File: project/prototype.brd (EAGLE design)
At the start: 76.2 x 38.1 mm, 10 parts, among them M1 NX7002AK, M2 NX3008PBK

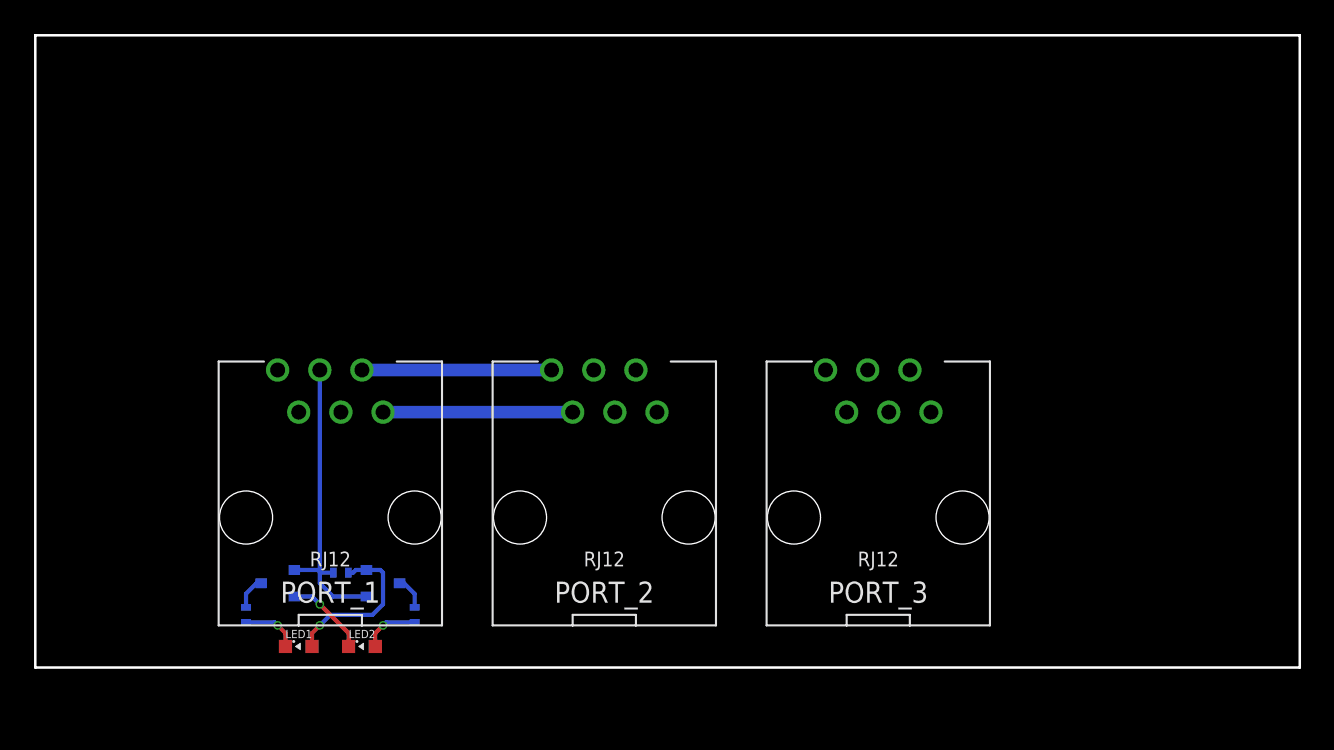
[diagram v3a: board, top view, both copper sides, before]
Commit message: Add input terminal blocks
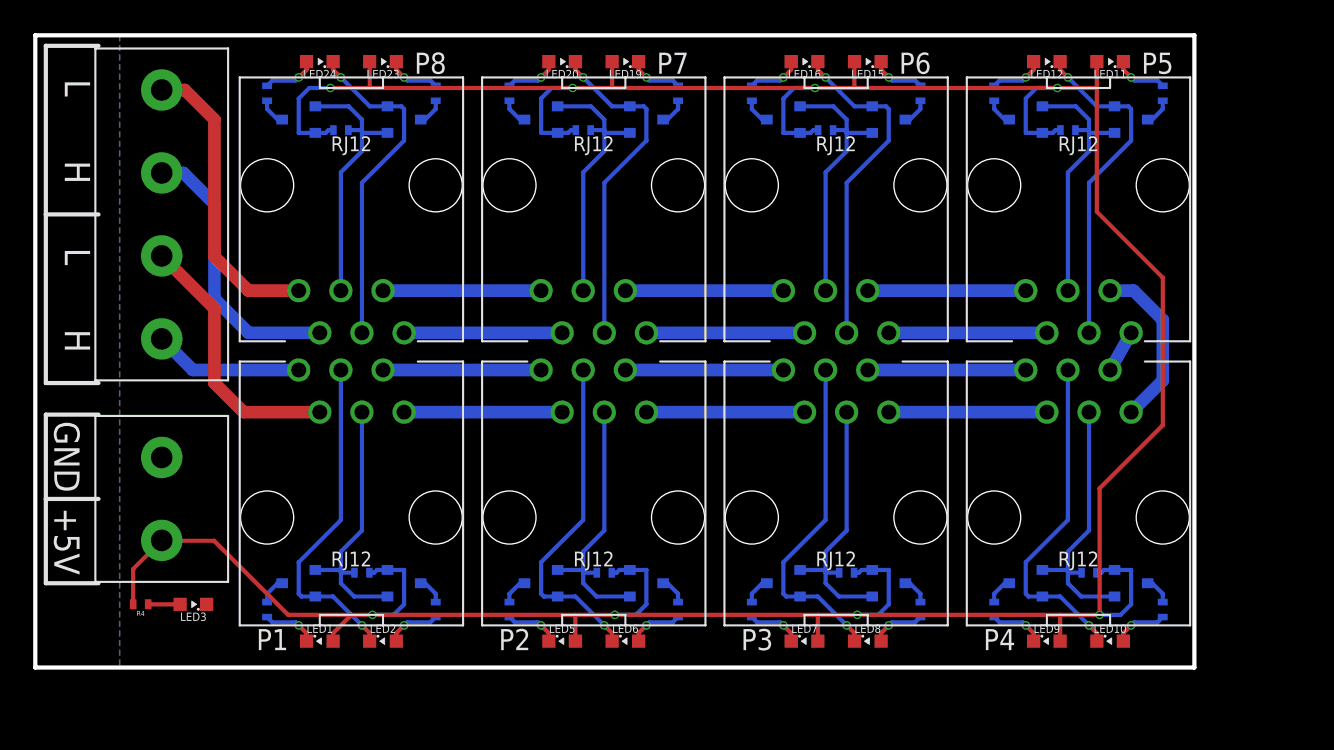
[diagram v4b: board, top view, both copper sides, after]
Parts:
- removed PORT_1, PORT_2, PORT_3: RJ12, components:RJ12
- added LED10, LED12, LED16, LED20, LED24, LED3, LED6, LED8: GREEN, components:0603-LED
- added LED11, LED15, LED19, LED23, LED5, LED7, LED9: RED, components:0603-LED
- added M10, M12, M16, M20, M24, M6, M8: NX7002AK, components:SOT23
- added M11, M15, M19, M23, M5, M7, M9: NX3008PBK, components:SOT23
- added P1, P2, P3, P4, P5, P6, P7, P8: RJ12, components:RJ12
- added R10, R13, R16, R22, R28, R34, R7: 10K, components:0402
- added R11, R12, R14, R15, R17, R18, R23, R24, R29, R30, R35, R36, R4, R8, R9: 130, components:0402
- added U$1: TERMINAL_BLOCK, components:TERMINALBLOCK-4
- added U$2: POWER_BLOCK, components:TERMINALBLOCK-2
- M1: value NX7002AK -> NX3008PBK
- M2: value NX3008PBK -> NX7002AK
- R1: value 130 -> 10K
- R3: value 10K -> 130
- moved R2 8.90 mm to (14.0, 3.49)
- moved M1 7.62 mm to (22.2, 5.08), turned to 90 degrees
- moved R1 7.43 mm to (19.7, 5.71), turned to 180 degrees
- moved R3 6.13 mm to (24.1, 3.49), turned to 90 degrees
- moved M2 5.08 mm to (15.9, 5.08), turned to 270 degrees
- moved LED1 1.31 mm to (17.1, 1.59)
- moved LED2 1.31 mm to (21.0, 1.59)
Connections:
- removed net CAN-H: PORT_1.1
- removed net CAN-L: PORT_1.2
- removed net GATE: M1.1, M2.1, PORT_1.3, R3.1
- removed net N$10: LED2.2, R2.1
- removed net N$2: M1.3, R1.2
- removed net N$3: PORT_1.5, PORT_2.1
- removed net N$5: PORT_3.5
- removed net N$6: PORT_1.6, PORT_2.2
- removed net N$7: PORT_2.5, PORT_3.1
- new net CAN_IN_H: P1.1, U$1.1
- new net CAN_IN_L: P1.2, U$1.2
- new net CAN_OUT_H: P8.5, U$1.3
- new net CAN_OUT_L: P8.6, U$1.4
- new net GATE1: M1.1, M2.1, P1.4, R1.1
- new net GATE11: M23.1, M24.1, P8.4, R34.1
- new net GATE2: M5.1, M6.1, P2.4, R7.1
- new net GATE3: M7.1, M8.1, P3.4, R10.1
- new net GATE4: M10.1, M9.1, P4.4, R13.1
- new net GATE5: M11.1, M12.1, P5.4, R16.1
- new net GATE7: M15.1, M16.1, P6.4, R22.1
- new net GATE9: M19.1, M20.1, P7.4, R28.1
- new net N$11: LED1.1, R2.1
- new net N$15: P1.5, P2.1
- new net N$16: M7.3, R12.2
- new net N$17: M5.3, R9.2
- new net N$18: LED6.2, R9.1
- new net N$19: LED5.1, R8.1
- new net N$20: M6.3, R8.2
- new net N$21: LED8.2, R12.1
- new net N$22: P1.6, P2.2
- new net N$23: P2.5, P3.1
- new net N$24: P2.6, P3.2
- new net N$25: LED7.1, R11.1
- new net N$26: M8.3, R11.2
- new net N$27: M11.3, R18.2
- new net N$28: LED12.2, R18.1
- new net N$29: P3.5, P4.1
- new net N$30: P3.6, P4.2
- new net N$31: M9.3, R15.2
- new net N$32: LED10.2, R15.1
- new net N$33: LED9.1, R14.1
- new net N$34: M10.3, R14.2
- new net N$35: LED11.1, R17.1
- new net N$36: M12.3, R17.2
- new net N$37: P4.5, P5.1
- new net N$38: P4.6, P5.2
- new net N$51: M15.3, R24.2
- new net N$52: LED16.2, R24.1
- new net N$53: LED15.1, R23.1
- new net N$54: M16.3, R23.2
- new net N$55: P5.5, P6.1
- new net N$56: P5.6, P6.2
- new net N$67: M19.3, R30.2
- new net N$68: LED20.2, R30.1
- new net N$69: LED19.1, R29.1
- new net N$70: M20.3, R29.2
- new net N$71: P6.5, P7.1
- new net N$72: P6.6, P7.2
- new net N$83: M23.3, R36.2
- new net N$84: LED24.2, R36.1
- new net N$85: LED23.1, R35.1
- new net N$86: M24.3, R35.2
- new net N$87: P7.5, P8.1
- new net N$88: P7.6, P8.2
- net +5V: now also LED11.2, LED15.2, LED19.2, LED23.2, LED5.2, LED7.2, LED9.2, M1.2, M11.2, M15.2, M19.2, M23.2, M5.2, M7.2, M9.2, R1.2, R10.2, R13.2, R16.2, R22.2, R28.2, R34.2, R4.2, R7.2, U$2.1; no longer M2.2, R3.2
- net GND: now also LED10.1, LED12.1, LED16.1, LED20.1, LED24.1, LED3.1, LED6.1, LED8.1, M10.2, M12.2, M16.2, M2.2, M20.2, M24.2, M6.2, M8.2, P1.3, P2.3, P3.3, P4.3, P5.3, P6.3, P7.3, P8.3, U$2.2; no longer M1.2, PORT_1.4, PORT_3.4
- net N$1: now also LED3.2, R4.1; no longer LED1.1, R1.1
- net N$8: now also M1.3, R3.2; no longer PORT_2.6, PORT_3.2
- net N$9: now also LED2.2, R3.1; no longer PORT_3.6
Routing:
- net +5V: track 9.93 -> 209.1 mm, vias 1 -> 8
- net GND: track 5.00 -> 162.3 mm, vias 1 -> 8
- net GATE: track 18.4 -> 0.00 mm
- net CAN_OUT_L: track 0.00 -> 18.1 mm
- net CAN_OUT_H: track 0.00 -> 16.9 mm
- net GATE5: track 0.00 -> 16.3 mm
- net GATE4: track 0.00 -> 16.3 mm
- net GATE7: track 0.00 -> 16.3 mm
- net GATE3: track 0.00 -> 16.3 mm
- net GATE11: track 0.00 -> 16.3 mm
- net GATE1: track 0.00 -> 16.3 mm
- net GATE9: track 0.00 -> 16.3 mm
- net GATE2: track 0.00 -> 16.3 mm
- net CAN_IN_L: track 0.00 -> 16.1 mm
- net N$6: track 11.4 -> 0.00 mm
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- added copper zone on layer 1, net GND
- added copper zone on layer 16, net GND
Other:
- board size 76.2 x 38.1 mm -> 69.8 x 38.1 mm
- board text added: "+5V"
- board text added: "Designed: RG"
- board text added: "GND"
- board text added: "H"
- board text added: "L"
- board text added: "Version 1.0"

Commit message: Change power LED layout
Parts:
- moved R4 4.45 mm to (10.8, 3.81), turned to 0 degrees
- moved LED3 1.27 mm to (8.26, 3.81), turned to 0 degrees
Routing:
- net +5V: track 209.1 -> 208.0 mm
- net N$1: track 1.92 -> 1.29 mm
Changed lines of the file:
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@@
 <element name="U$1" library="components" package="TERMINALBLOCK-4" value="TERMINAL_BLOCK" x="7.62" y="27.305" smashed="yes" rot="R90"/>
 <element name="U$2" library="components" package="TERMINALBLOCK-2" value="POWER_BLOCK" x="7.62" y="10.16" smashed="yes" rot="R90"/>
-<element name="R4" library="components" package="0402" value="130" x="6.35" y="3.81" smashed="yes" rot="R180">
-<attribute name="NAME" x="6.35" y="3.41" size="0.3" layer="25" font="vector" rot="R180" align="bottom-center"/>
-<attribute name="VALUE" x="6.35" y="4.21" size="0.15" layer="27" font="vector" align="bottom-center"/>
+<element name="R4" library="components" package="0402" value="130" x="10.795" y="3.81" smashed="yes">
+<attribute name="NAME" x="10.795" y="4.21" size="0.3" layer="25" font="vector" align="bottom-center"/>
+<attribute name="VALUE" x="10.795" y="3.41" size="0.15" layer="27" font="vector" rot="R180" align="bottom-center"/>
 </element>
-<element name="LED3" library="components" package="0603-LED" value="GREEN" x="9.525" y="3.81" smashed="yes" rot="R180">
-<attribute name="NAME" x="9.525" y="3.31" size="0.5" layer="25" font="vector" rot="R180" align="bottom-center"/>
-<attribute name="VALUE" x="9.525" y="4.31" size="0.35" layer="27" font="vector" align="bottom-center"/>
+<element name="LED3" library="components" package="0603-LED" value="GREEN" x="8.255" y="3.81" smashed="yes">
+<attribute name="NAME" x="8.255" y="4.31" size="0.5" layer="25" font="vector" align="bottom-center"/>
+<attribute name="VALUE" x="8.255" y="3.31" size="0.35" layer="27" font="vector" rot="R180" align="bottom-center"/>
 </element>
 </elements>
@@
 <contactref element="R4" pad="2"/>
 <wire x1="7.62" y1="7.66" x2="7.6" y2="7.64" width="0.254" layer="1"/>
-<wire x1="7.6" y1="7.64" x2="5.9" y2="5.94" width="0.254" layer="1"/>
-<wire x1="5.9" y1="5.94" x2="5.9" y2="3.81" width="0.254" layer="1"/>
 <wire x1="19.05" y1="3.175" x2="15.24" y2="3.175" width="0.254" layer="1"/>
 <wire x1="10.775" y1="7.64" x2="7.6" y2="7.64" width="0.254" layer="1"/>
-<wire x1="15.24" y1="3.175" x2="10.775" y2="7.64" width="0.254" layer="1"/>
+<wire x1="14.605" y1="3.81" x2="10.775" y2="7.64" width="0.254" layer="1"/>
 <wire x1="64.135" y1="3.175" x2="64.135" y2="10.795" width="0.254" layer="1"/>
 <wire x1="64.135" y1="10.795" x2="67.945" y2="14.605" width="0.254" layer="1"/>
@@
 <wire x1="63.97" y1="34.925" x2="63.97" y2="36.5125" width="0.254" layer="1"/>
 <wire x1="61.595" y1="34.925" x2="63.97" y2="34.925" width="0.254" layer="1"/>
+<wire x1="11.245" y1="3.81" x2="14.605" y2="3.81" width="0.254" layer="1"/>
+<wire x1="14.605" y1="3.81" x2="15.24" y2="3.175" width="0.254" layer="1"/>
 </signal>
 <signal name="N$8">
@@
 <contactref element="R4" pad="1"/>
 <contactref element="LED3" pad="2"/>
-<wire x1="6.8" y1="3.81" x2="8.725" y2="3.81" width="0.254" layer="1"/>
+<wire x1="9.055" y1="3.81" x2="10.345" y2="3.81" width="0.254" layer="1"/>
 </signal>
 </signals>
